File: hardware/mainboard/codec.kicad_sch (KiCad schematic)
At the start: 106 parts, among them U10 Opamp_Quad, U12 OPA2365AID, U17 OPA2188AIDR, U18 TAC5242IRGER, U5 Opamp_Quad, Y1 ASDMB-24.576MHZ-LY-T

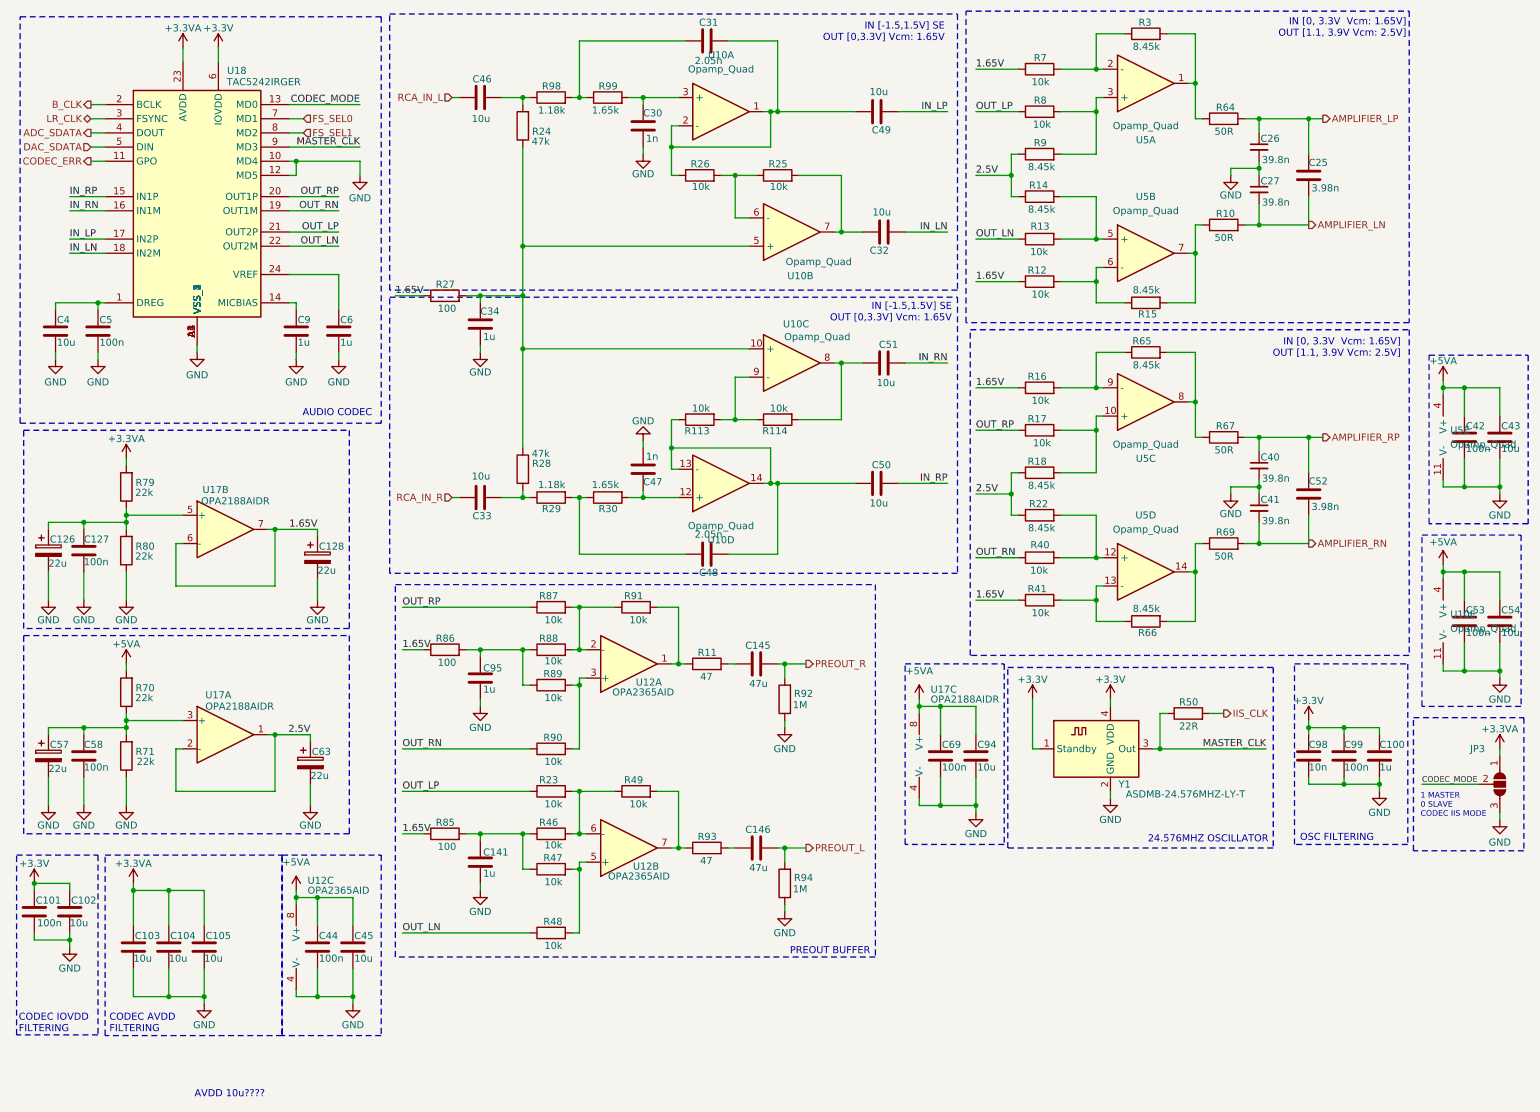
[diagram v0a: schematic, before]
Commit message: Add power supply and front panel PCBs
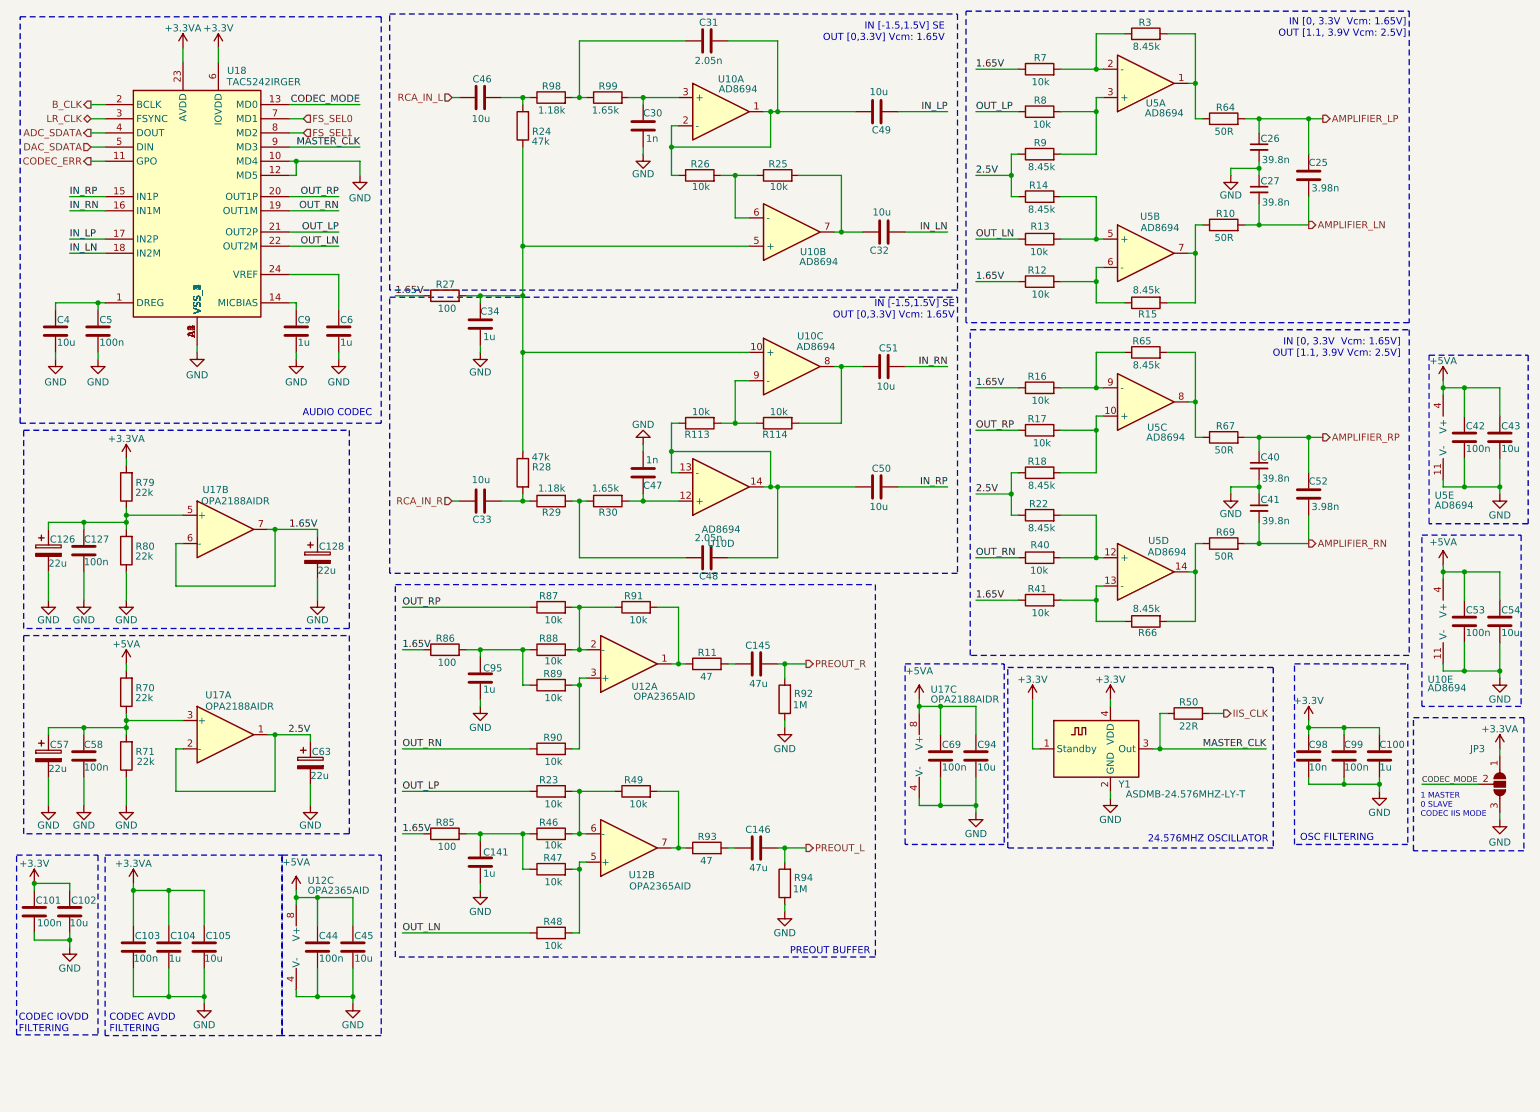
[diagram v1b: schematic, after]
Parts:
- C103: value 10u -> 100n
- C104: value 10u -> 1u
- U10, U5: value Opamp_Quad -> AD8694
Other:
- note removed: "AVDD 10u????"
- moved on the sheet: C33, C47, C48, C50, C51, R113, R114, R28, R29, R30, U10C, U10D

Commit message: Prepare PCB for production
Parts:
- C100, C104, C34, C6, C9: Manufacturer_Part_Number (none) -> CL10A105KB8NNNC
- C101, C103, C127, C42, C44, C5, C53, C58, C69, C99: Manufacturer_Part_Number (none) -> 0603B104K500CT
- C102, C105, C4, C43, C45, C54, C94: Manufacturer_Part_Number (none) -> GRM188R61E106KA73J
- C126, C128, C57, C63: Manufacturer_Part_Number (none) -> 293D226X9010A2TE3
- C141, C95: Manufacturer_Part_Number (none) -> CL21B105KAFNNNE
- C145, C146: Manufacturer_Part_Number (none) -> CL21A476MQYNNNE
- C25, C52: Manufacturer_Part_Number (none) -> GCM1885C1H392JA16D
- C26, C27, C40, C41: Manufacturer_Part_Number (none) -> C0603C393K5RACTU
- C30, C47: Manufacturer_Part_Number (none) -> 0603B102K500CT
- C31, C48: Manufacturer_Part_Number (none) -> GCM188R71H272KA37D
- C32, C33, C46, C49, C50, C51: Manufacturer_Part_Number (none) -> GRM21BR61E106KA73L
- C98: Manufacturer_Part_Number (none) -> 06035C103KAT2A
- R10, R64, R67, R69: Manufacturer_Part_Number (none) -> AR03BTCX0500
- R11, R93: Manufacturer_Part_Number (none) -> RC0603JR-0747RL
- R113, R114, R12, R13, R16, R17, R23, R25, R26, R40, R41, R46, R47, R48, R49, R7, R8, R87, R88, R89, R90, R91: Manufacturer_Part_Number (none) -> RC0603JR-0710KL
- R14, R15, R18, R22, R3, R65, R66, R9: Manufacturer_Part_Number (none) -> ERA3AEB8661V
- R24, R28: Manufacturer_Part_Number (none) -> RC0603JR-0747KL
- R27, R85, R86: Manufacturer_Part_Number (none) -> WR06X101 JTL
- R29, R98: Manufacturer_Part_Number (none) -> ERA3AEB1181V
- R30, R99: Manufacturer_Part_Number (none) -> ERA3AEB1651V
- R50: Manufacturer_Part_Number (none) -> WR06X220 JTL
- R70, R71, R79, R80: Manufacturer_Part_Number (none) -> WR06X2202FTL
- R92, R94: Manufacturer_Part_Number (none) -> RC0603JR-071ML
- U10, U5: Manufacturer_Part_Number (none) -> AD8694; now left out of the parts list
- U12: Manufacturer_Part_Number (none) -> OPA2365AID
- U17: Manufacturer_Part_Number (none) -> OPA2188AIDR
- Y1: Manufacturer_Part_Number (none) -> ASDMB-24.576MHZ-LY-T
